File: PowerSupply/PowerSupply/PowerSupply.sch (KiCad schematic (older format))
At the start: 33 parts

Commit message: pcb updates
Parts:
- removed J?: touchLCD, symbol CustomComponents:touchLCD
- removed R?: Rsense, symbol Device:R
- added F1, F2, F3: Polyfuse, Fuse:Fuse_1206_3216Metric, symbol Device:Polyfuse
- added H1: 5V_load, TestPoint:TestPoint_Pad_D2.5mm, symbol Mechanical:MountingHole_Pad
- added H2: 5V_load_GND, TestPoint:TestPoint_Pad_D2.5mm, symbol Mechanical:MountingHole_Pad
- added H3: 5V_USB, TestPoint:TestPoint_Pad_D2.5mm, symbol Mechanical:MountingHole_Pad
- added H4: 5V_OUT, MountingHole:MountingHole_2.2mm_M2_Pad_Via, symbol Mechanical:MountingHole_Pad
- added H5: 12V_OUT, MountingHole:MountingHole_2.2mm_M2_Pad_Via, symbol Mechanical:MountingHole_Pad
- added H6: 3p3V_OUT, MountingHole:MountingHole_2.2mm_M2_Pad_Via, symbol Mechanical:MountingHole_Pad
- added H7: GND_OUT, MountingHole:MountingHole_2.2mm_M2_Pad_Via, symbol Mechanical:MountingHole_Pad
- added J1: Conn_01x04_Female, Connectors2:1X04, symbol Connector:Conn_01x04_Female
- added J2: ATX24, Connector_Molex:Molex_Mini-Fit_Jr_5566-24A_2x12_P4.20mm_Vertical, symbol atx24:ATX24
- added J3: PS_ON, Connectors2:1X02, symbol Connector:Conn_01x02_Female
- added R14, R15: R, Resistors_SMD:R_0805, symbol Device:R
- added U6: R_0612, Resistor_SMD:R_Shunt_Vishay_WSKW0612, symbol CustomComponents:R_0612
- added U7: ATmega328P-AU, Package_QFP:TQFP-32_7x7mm_P0.8mm, symbol MCU_Microchip_ATmega:ATmega328P-AU
- A1: renamed from A?; footprint Module:Arduino_Nano -> CustomPS:arduino_nano
- C1, C2, C3, C4: renamed from C?; footprint (none) -> Capacitors:0805
- P1: renamed from P?; footprint (none) -> CustomPS:uMAX-uSOP_10
- Q1: renamed from Q?; footprint (none) -> SMD_Packages:SO-8_PowerPAK_Vishay_Single
- Q2, Q3, Q4: renamed from Q?; footprint (none) -> kicad-open-modules:PowerPAK-1212-8
- Q5, Q6, Q7, Q8: renamed from Q?; footprint Package_TO_SOT_SMD:SOT-23 -> SMD_Packages_oj:SOT23
- R1, R10, R11, R12, R13, R2, R3, R4, R5, R6, R7, R9: renamed from R?; footprint (none) -> Resistors_SMD:R_0805
- U1, U2, U3: renamed from U?; value ACS70331EESATR-005U3 -> ACS70331; footprint ALLEGRO_ACS70331EESATR-005U3 -> ACS70331EESATR-005U3:ALLEGRO_ACS70331EESATR-005U3
- U4: renamed from U?; footprint 21-0140L_T2855-3 -> CustomFP:MAX11136ATI&plus_
- U5: renamed from U?; footprint 21-0036K -> CustomFP:MAX6126B30&plus_
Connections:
- net 5V_DIV_Out is gone; now on net 5V_DIV_OUT: R1.2, R2.1
- net +12V: now also F3.1, J2.10 (12V), J2.11 (12V); no longer U3.1 (IP+), U3.2 (IP+)
- net +3V3: now also A1.30 (VIN), F1.1, J1.4 (Pin_4), J2.1 (3V3), J2.12 (3V3), J2.13 (3V3), J2.2 (3V3); no longer P1.5 (INA+), U1.1 (IP+), U1.2 (IP+)
- net 12V_EN: now also A1.8 (D5)
- net 12V_Out: now also H5.1
- net 3V3_COURSE_EN: now also A1.10 (D7)
- net 3V3_FINE_EN: now also A1.11 (D8)
- net 3V3_Out: now also H6.1
- net 5V_DIV_OUT: now also U4.2 (AIN4); no longer U4.1 (AIN3)
- net 5V_EN: now also A1.9 (D6)
- net 5V_Out: now also H4.1
- net CNVST_PINX: now also A1.7 (D4)
- net EOC_PINX: now also A1.6 (D3)
- net GND: now also A1.4 (GND), H2.1, H7.1, J1.3 (Pin_3), J2.15 (GND), J2.19 (GND), J2.7 (GND), R14.2
- net SPI_3V3_CS_PINX: now also A1.12 (D9)
- net SPI_ADC_CS_PINX: now also A1.13 (D10)
- net SPI_Clk_PINX: now also A1.16 (D13)
- net SPI_MISO_PINX: now also A1.15 (D12)
- net SPI_MOSI_PINX: now also A1.14 (D11)
- net at A1.1 (D1/TX): now also J1.1 (Pin_1)
- net POK: now reaches A1.19 (A0)
- net POK: now also R14.1, R15.1
- net at A1.2 (D0/RX): now also J1.2 (Pin_2)
- net 3.3VA_D2: now reaches Q3.3 (Drain), U1.3 (IP-), U1.4 (IP-)
- net at U2.10 (VIOUT): now also U4.4 (AIN6); no longer U4.2 (AIN4)
- net at U4.27 (AIN1): no longer P1.8 (OUTA)
- net at U3.10 (VIOUT): now also U4.5 (AIN7); no longer U4.4 (AIN6)
- net at P1.4 (INA-): now also U6.3 (S-); no longer Q2.3 (Drain)
- net 5VA_D: now reaches Q4.3 (Drain), U2.3 (IP-), U2.4 (IP-)
- net 12VA_S: now reaches Q1.2 (Source), U3.3 (IP-), U3.4 (IP-)
- net +5V renamed 5V_A
- net 5V_A: now also F2.2
- new net: P1.5 (INA+), U6.2 (S+)
- new net: J2.16 (PS_ON), J3.1 (Pin_1)
- new net: J2.17 (GND), J3.2 (Pin_2)
- new net: H1.1, J2.21 (5V)
- new net: J2.8 (POK), R15.2
- new net: U7.21 (GND), U7.3 (GND), U7.5 (GND)
- new net: U7.4 (VCC), U7.6 (VCC)
- new net 12V_A: F3.2, U3.1 (IP+), U3.2 (IP+)
- new net 3.3VA_D1: Q2.3 (Drain), U6.4 (P-)
- new net 3.3V_A: F1.2, U1.1 (IP+), U1.2 (IP+), U6.1 (P+)
- new net 3V3_Fine_Out: P1.8 (OUTA), U4.1 (AIN3)
- new net 5VA: F2.1, J2.4 (5V), J2.6 (5V)
- new net 5V_USB: H3.1, J2.9 (5VSB)
- no-connect marks 3 -> 23
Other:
- moved on the sheet: A1

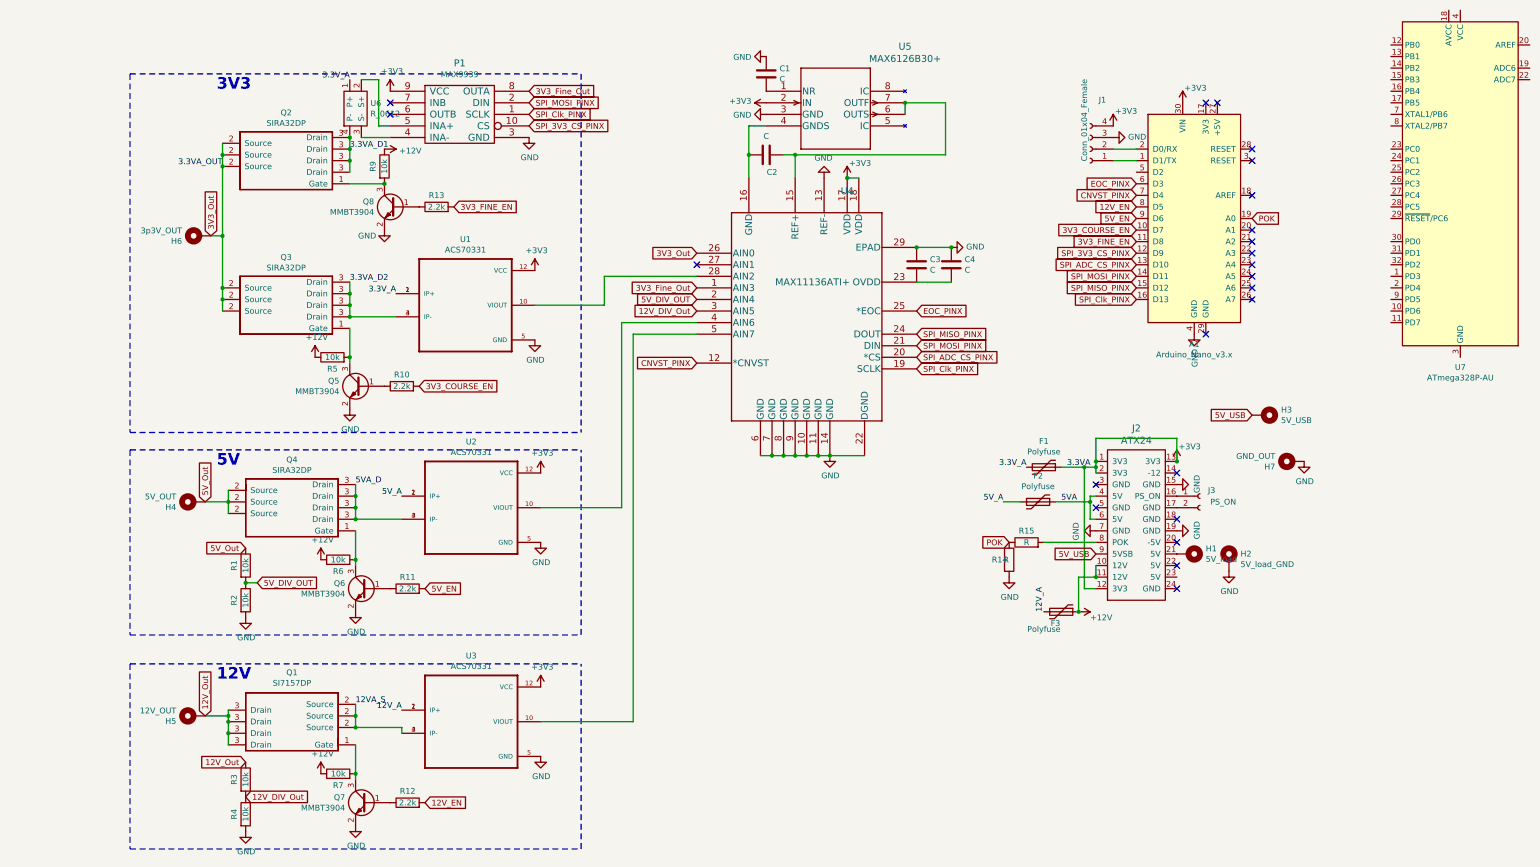
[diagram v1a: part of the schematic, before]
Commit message: Updated Door Unlocker and PS
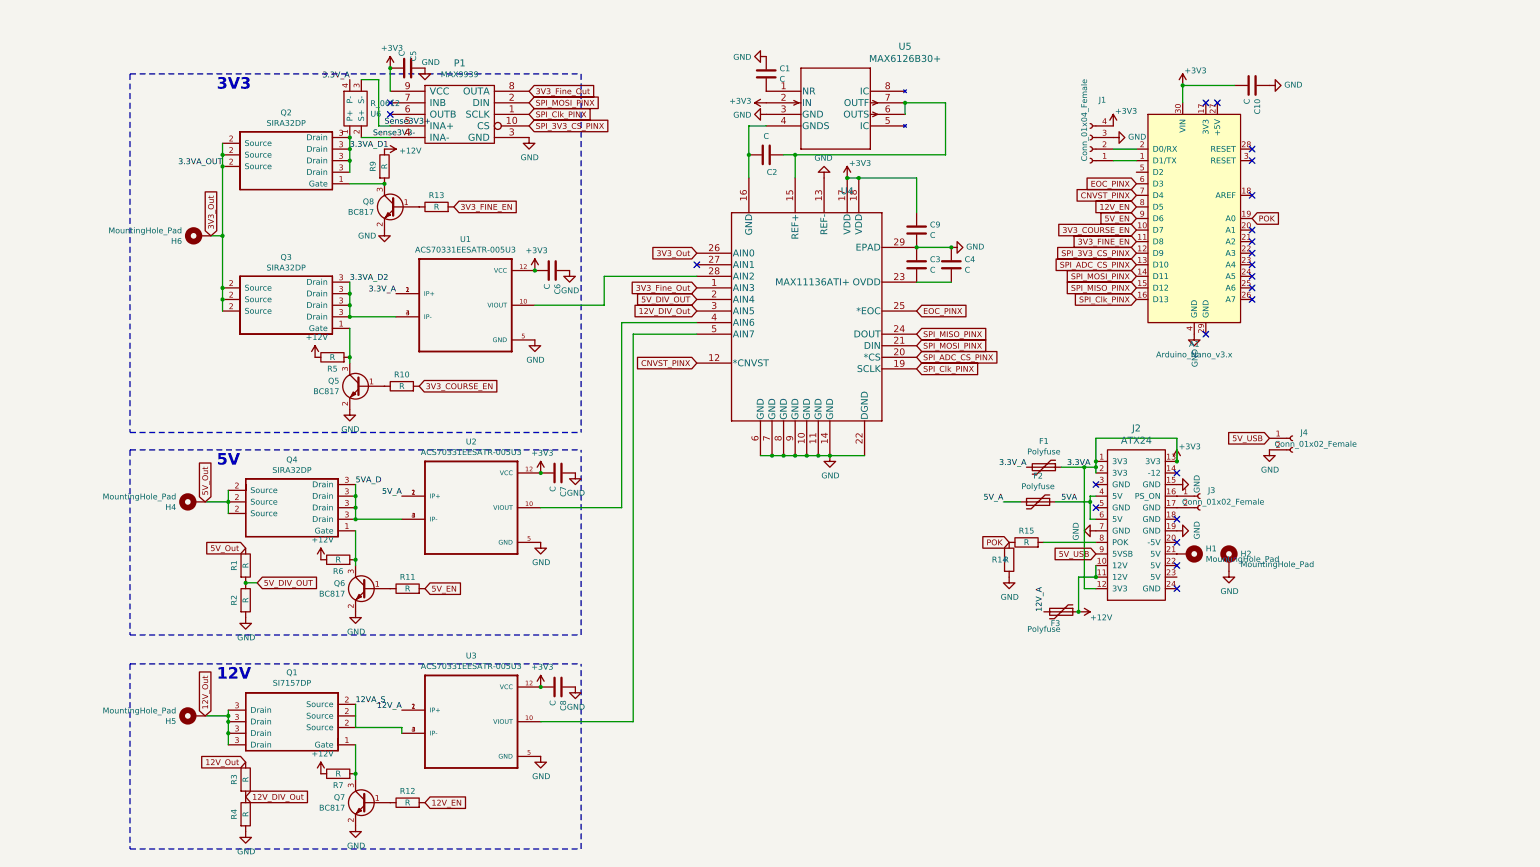
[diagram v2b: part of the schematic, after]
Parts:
- removed H3: 5V_USB, TestPoint:TestPoint_Pad_D2.5mm, symbol Mechanical:MountingHole_Pad
- removed H7: GND_OUT, MountingHole:MountingHole_2.2mm_M2_Pad_Via, symbol Mechanical:MountingHole_Pad
- removed U7: ATmega328P-AU, Package_QFP:TQFP-32_7x7mm_P0.8mm, symbol MCU_Microchip_ATmega:ATmega328P-AU
- added C10, C5, C6, C7, C8, C9: C, Capacitor_SMD:C_0805_2012Metric, symbol Device:C
- added J4: Conn_01x02_Female, Connector_PinHeader_2.54mm:PinHeader_1x02_P2.54mm_Vertical, symbol Connector:Conn_01x02_Female
- A1: footprint CustomPS:arduino_nano -> Module:Arduino_Nano
- C1, C2, C3, C4: footprint Capacitors:0805 -> Capacitor_SMD:C_0805_2012Metric
- F1, F2, F3: footprint Fuse:Fuse_1206_3216Metric -> Resistor_SMD:R_1206_3216Metric
- H1: value 5V_load -> MountingHole_Pad; footprint TestPoint:TestPoint_Pad_D2.5mm -> MountingHole:MountingHole_2.2mm_M2
- H2: value 5V_load_GND -> MountingHole_Pad; footprint TestPoint:TestPoint_Pad_D2.5mm -> MountingHole:MountingHole_2.2mm_M2_Pad_Via
- H4: value 5V_OUT -> MountingHole_Pad
- H5: value 12V_OUT -> MountingHole_Pad
- H6: value 3p3V_OUT -> MountingHole_Pad
- J1: footprint Connectors2:1X04 -> Connector_PinHeader_2.54mm:PinHeader_1x04_P2.54mm_Vertical
- J2: footprint Connector_Molex:Molex_Mini-Fit_Jr_5566-24A_2x12_P4.20mm_Vertical -> CustomPS:ATX_24Pin
- J3: value PS_ON -> Conn_01x02_Female; footprint Connectors2:1X02 -> Connector_PinHeader_2.54mm:PinHeader_1x02_P2.54mm_Vertical
- Q1: footprint SMD_Packages:SO-8_PowerPAK_Vishay_Single -> CustomPS:Vishay_PowerPAK_SO-8
- Q2, Q3, Q4: footprint kicad-open-modules:PowerPAK-1212-8 -> CustomPS:Vishay_PowerPAK_SO-8
- Q5, Q6, Q7, Q8: value MMBT3904 -> BC817; footprint SMD_Packages_oj:SOT23 -> Package_TO_SOT_SMD:SOT-23
- R1, R2, R3, R4, R5, R6, R7, R9: value 10k -> R; footprint Resistors_SMD:R_0805 -> Resistor_SMD:R_0805_2012Metric
- R10, R11, R12, R13: value 2.2k -> R; footprint Resistors_SMD:R_0805 -> Resistor_SMD:R_0805_2012Metric
- R14, R15: footprint Resistors_SMD:R_0805 -> Resistor_SMD:R_0805_2012Metric
- U1, U2, U3: value ACS70331 -> ACS70331EESATR-005U3
- U5: footprint CustomFP:MAX6126B30&plus_ -> Package_SO:MSOP-8_3x3mm_P0.65mm
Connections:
- net +3V3: now also C10.2, C5.2, C6.2, C7.2, C8.2, C9.1
- net 3.3VA_D1: now also U6.1 (P+); no longer U6.4 (P-)
- net 3.3V_A: now also U6.4 (P-); no longer U6.1 (P+)
- net 5V_USB: now also J4.1 (Pin_1)
- net GND: now also C10.1, C5.1, C6.1, C7.1, C8.1, C9.2, J4.2 (Pin_2)
- net Sense3V3+: now reaches U6.3 (S-)
- net Sense3V3+: now also P1.5 (INA+); no longer P1.4 (INA-)
- net Sense3V3-: now reaches U6.2 (S+)
- net Sense3V3-: now also P1.4 (INA-); no longer P1.5 (INA+)
